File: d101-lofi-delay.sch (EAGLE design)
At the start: 84 parts, among them U1 FX2-20P-1.27DS, U2 FX2-20S-1.27DS

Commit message: Add Knobs
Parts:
- added O2, O3, O4: 450-AA150(15MM,D,BLACK), hardware:450-AA150(15MM,D,BLACK)
- added O5: 450-CP155(15MM,GRAY/WHITE), hardware:450-CP155(15MM,GRAY/WHITE)
- added O6, O7: 450-CP157(15MM,WHITE/BLACK), hardware:450-CP157(15MM,WHITE/BLACK)
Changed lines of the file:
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@@
 <?xml version="1.0" encoding="utf-8"?>
 <!DOCTYPE eagle SYSTEM "eagle.dtd">
-<eagle version="7.4.1">
+<eagle version="7.5.1">
 <drawing>
 <settings>
@@
 <part name="GND24" library="supply" deviceset="GND" device=""/>
 <part name="SA2" library="switches" deviceset="MJS22R" device=""/>
+<part name="O2" library="hardware" deviceset="450-AA?" device="150(15MM,D,BLACK)"/>
+<part name="O3" library="hardware" deviceset="450-AA?" device="150(15MM,D,BLACK)"/>
+<part name="O4" library="hardware" deviceset="450-AA?" device="150(15MM,D,BLACK)"/>
+<part name="O5" library="hardware" deviceset="450-C?" device="P155(15MM,GRAY/WHITE)"/>
+<part name="O6" library="hardware" deviceset="450-C?" device="P157(15MM,WHITE/BLACK)"/>
+<part name="O7" library="hardware" deviceset="450-C?" device="P157(15MM,WHITE/BLACK)"/>
 </parts>
 <sheets>
@@
 <instance part="SA2" gate=".1" x="215.9" y="12.7" rot="MR0"/>
 <instance part="SA2" gate=".2" x="215.9" y="-114.3" rot="MR0"/>
+<instance part="O2" gate="G$1" x="55.88" y="-119.38"/>
+<instance part="O3" gate="G$1" x="289.56" y="-66.04"/>
+<instance part="O4" gate="G$1" x="287.02" y="-193.04"/>
+<instance part="O5" gate="G$1" x="55.88" y="-119.38"/>
+<instance part="O6" gate="G$1" x="289.56" y="-66.04"/>
+<instance part="O7" gate="G$1" x="287.02" y="-193.04"/>
 </instances>
 <busses>

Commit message: Add Knobs
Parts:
- removed C34, C35: 100N, capacitors:100N
- removed C36, C37: 47N(FILM), capacitors:47N(FILM)
- removed C38, C39: 33U/25V, capacitors-electrolytic:33U/25V
- removed O7: 450-CP157(15MM,WHITE/BLACK), hardware:450-CP157(15MM,WHITE/BLACK)
- removed R36, R37, R38, R39: 10K, resistors:10K
- removed R41, R43, R44, R45: 1K, resistors:1K
- added C10, C11: 10N(FILM), capacitors:10N(FILM)
- added C12, C13: 100N, capacitors:100N
- added C8, C9: 100N(FILM), capacitors:100N(FILM)
- added R12, R13, R22, R23: 15K, resistors:15K
- added R14: 1K, resistors:1K
- added R21, R24, R25: 10K, resistors:10K
- added U10: FX2-20S-1.27DS, hardware:FX2-20S-1.27DS
- added U11, U12: D-SHAFT-ADAPTER, hardware:D-SHAFT-ADAPTER
- added U3, U4, U8, U9: NUT-M2-SELFLOCK, hardware:NUT-M2-SELFLOCK
- added U5: FX2-20P-1.27DS, hardware:FX2-20P-1.27DS
- added U6, U7: SCREW-M2X8, hardware:SCREW-M2X8
- C14, C15: value 100N(FILM) -> 2N2(FILM); device capacitors:100N(FILM) -> capacitors:2N2(FILM)
- C16, C17: value 10N(FILM) -> 10U/35V; device capacitors:10N(FILM) -> capacitors-electrolytic:10U/35V
- C18, C19: value 100N -> 2N2(FILM); device capacitors:100N -> capacitors:2N2(FILM)
- C20, C21: value 2N2(FILM) -> 100N(FILM); device capacitors:2N2(FILM) -> capacitors:100N(FILM)
- C22, C23: value 10U/35V -> 10N(FILM); device capacitors-electrolytic:10U/35V -> capacitors:10N(FILM)
- C24, C25: value 2N2(FILM) -> 100N; device capacitors:2N2(FILM) -> capacitors:100N
- C28, C29: value 10N(FILM) -> 100N; device capacitors:10N(FILM) -> capacitors:100N
- C30, C31: value 100N -> 47N(FILM); device capacitors:100N -> capacitors:47N(FILM)
- C32, C33: value 100N(FILM) -> 33U/25V; device capacitors:100N(FILM) -> capacitors-electrolytic:33U/25V
- O1: value (none) -> 450-AA150(15MM,D,BLACK); device text:TITLE -> hardware:450-AA150(15MM,D,BLACK)
- O2: value 450-AA150(15MM,D,BLACK) -> 450-CP155(15MM,GRAY/WHITE); device hardware:450-AA150(15MM,D,BLACK) -> hardware:450-CP155(15MM,GRAY/WHITE)
- O4: value 450-AA150(15MM,D,BLACK) -> 450-CP157(15MM,WHITE/BLACK); device hardware:450-AA150(15MM,D,BLACK) -> hardware:450-CP157(15MM,WHITE/BLACK)
- O5: value 450-CP155(15MM,GRAY/WHITE) -> 450-AA150(15MM,D,BLACK); device hardware:450-CP155(15MM,GRAY/WHITE) -> hardware:450-AA150(15MM,D,BLACK)
- PCB1: value rev.A -> D101 rev.A
- R15, R32: value 15K -> 1K; device resistors:15K -> resistors:1K
- R16: value 15K -> 100K; device resistors:15K -> resistors:100K
- R17: value 1K -> 100K; device resistors:1K -> resistors:100K
- R18: value 1K -> 10K; device resistors:1K -> resistors:10K
- R19, R20: value B50K** -> 10K; device potentiometers:B50K** -> resistors:10K
- R26, R27: value 100K -> 10K; device resistors:100K -> resistors:10K
- R30, R34, R35: value 10K -> 1K; device resistors:10K -> resistors:1K
- R31: value 10K -> B50K**; device resistors:10K -> potentiometers:B50K**
- R33: value 15K -> B50K**; device resistors:15K -> potentiometers:B50K**
- U1: value FX2-20P-1.27DS -> SCREW-M2X8; device hardware:FX2-20P-1.27DS -> hardware:SCREW-M2X8
- U2: value FX2-20S-1.27DS -> SCREW-M2X8; device hardware:FX2-20S-1.27DS -> hardware:SCREW-M2X8
- renumbered SA2 to SA1
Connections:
- net +5V: now also C12.2, C13.2; no longer C18.2, C19.2
- net FBK_INT_LEFT: now also R12.2; no longer R15.2
- net FBK_INT_RIGHT: now also R13.2; no longer R16.2
- net GND: now also C10.1, C11.1, C12.1, C13.1, C16.-, C17.-, C22.1, C23.1, C24.1, C25.1, R16.1, R17.1, R31.CW, R31.W, R33.CW, R33.W, VD1.C, VD4.A; no longer C16.1, C17.1, C18.1, C19.1, C22.-, C23.-, C34.1, C35.1, C36.1, C37.1, R19.CW, R19.W, R20.CW, R20.W, R26.1, R27.1, VD1.A, VD4.C
- net N$1: now also R32.1, R33.CCW; no longer R19.CCW, R43.1
- net N$10: now also C11.2, R19.2, R21.2, R23.2; no longer C17.2, R29.2, R31.2, R33.2
- net N$13: now also R15.1; no longer R18.1
- net N$15: now also C23.2, R25.2, R27.2, R29.2; no longer C29.2, R35.2, R37.2, R39.2
- net N$17: now also C15.2, R23.1; no longer C21.2, R33.1
- net N$18: now also C19.1, R25.1; no longer C25.1, R45.1
- net N$19: now also C19.2, R27.1; no longer C25.2, R37.1
- net N$2: now also R30.1, R31.CCW; no longer R20.CCW, R41.1
- net N$20: now also C21.1, R29.1; no longer C27.1, R39.1
- net N$21: now also C21.2; no longer C27.2
- net N$22: now also C27.1; no longer C33.1
- net N$23: now also C27.2; no longer C33.2
- net N$24: now also C31.2, C33.+, R35.2; no longer C37.2, C39.+, R45.2
- net N$25: now also R13.1; no longer R16.1
- net N$28: now also R3.1; no longer R7.1
- net N$3: now also C9.1, R14.2, VD1.A, VD3.C; no longer C15.1, R17.2, VD1.C, VD2.A
- net N$30: now also R7.1; no longer R2.1
- net N$31: now also C25.2; no longer C31.2
- net N$32: now also C29.2; no longer C35.2
- net N$33: now also R32.2; no longer R43.2
- net N$37: now also C17.+; no longer C23.+
- net N$39: now also R10.2; no longer R8.2
- net N$4: now also C15.1, R21.1; no longer C21.1, R31.1
- net N$40: now also R4.2; no longer R10.2
- net N$48: now also C22.2, R24.2, R26.2, R28.2; no longer C28.2, R34.2, R36.2, R38.2
- net N$49: now also C14.1, R20.1; no longer C20.1, R30.1
- net N$5: now also C8.1, R15.2, VD2.A, VD4.C; no longer C14.1, R18.2, VD3.C, VD4.A
- net N$50: now also C14.2, R22.1; no longer C20.2, R32.1
- net N$51: now also C18.1, R24.1; no longer C24.1, R44.1
- net N$52: now also C18.2, R26.1; no longer C24.2, R36.1
- net N$53: now also C20.1, R28.1; no longer C26.1, R38.1
- net N$54: now also C20.2; no longer C26.2
- net N$55: now also C26.1; no longer C32.1
- net N$56: now also C26.2; no longer C32.2
- net N$57: now also C30.2, C32.+, R34.2; no longer C36.2, C38.+, R44.2
- net N$58: now also C24.2; no longer C30.2
- net N$59: now also C28.2; no longer C34.2
- net N$6: now also R14.1; no longer R17.1
- net N$60: now also R30.2; no longer R41.2
- net N$61: now also R7.2, R8.2; no longer R2.2, R4.2
- net N$62: now also C8.2, R16.2, R18.1; no longer C14.2, R26.2, R28.1
- net N$63: now also C10.2, R18.2, R20.2, R22.2; no longer C16.2, R28.2, R30.2, R32.2
- net N$64: now also R12.1; no longer R15.1
- net N$65: now also R2.2, R8.1; no longer R3.2, R4.1
- net N$69: now also C16.+; no longer C22.+
- net N$7: now also R10.1, R3.2; no longer R7.2, R8.1
- net N$9: now also C9.2, R17.2, R19.1; no longer C15.2, R27.2, R29.1
- net OUT_LEFT: now also C33.-, R4.1; no longer C39.-, R10.1
- net OUT_RIGHT: now also C32.-, R2.1; no longer C38.-, R3.1
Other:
- moved on the sheet: C14, C15, C18, C19, C20, C21, C24, C25, C26, C27, C28, C29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

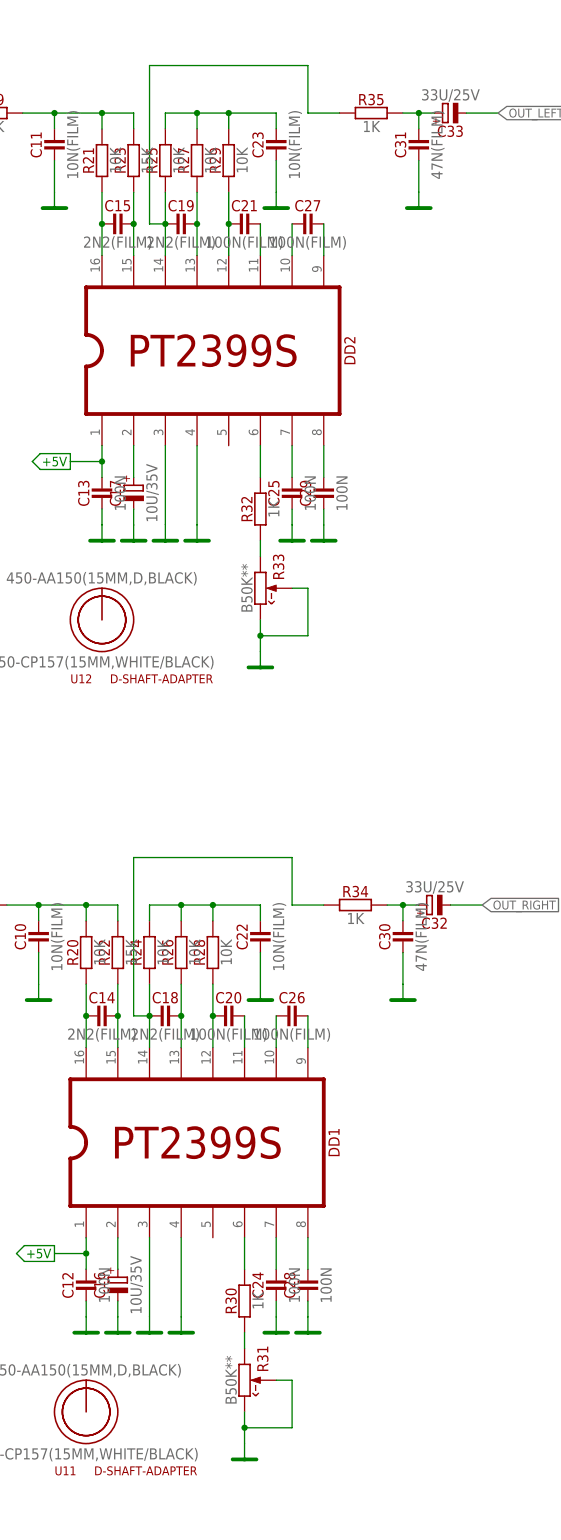
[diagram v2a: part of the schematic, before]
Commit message: D101 Update
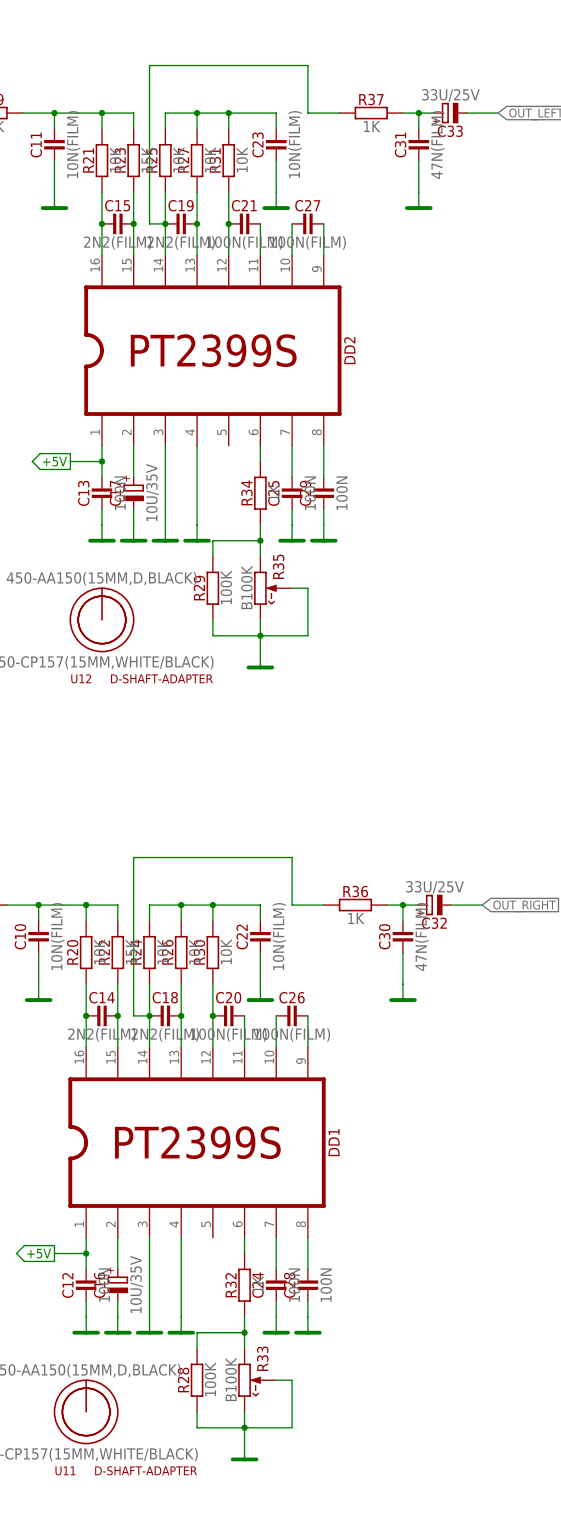
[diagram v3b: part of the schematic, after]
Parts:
- added R36, R37: 1K, resistors:1K
- R28, R29: value 10K -> 100K; device resistors:10K -> resistors:100K
- R30: value 1K -> 10K; device resistors:1K -> resistors:10K
- R31: value B50K** -> 10K; device potentiometers:B50K** -> resistors:10K
- R33: value B50K** -> B100K; device potentiometers:B50K** -> potentiometers:B100K
- R35: value 1K -> B100K; device resistors:1K -> potentiometers:B100K
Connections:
- net GND: now also R28.1, R29.1, R35.CW, R35.W; no longer R31.CW, R31.W
- net N$1: now also R29.2, R34.1, R35.CCW; no longer R32.1, R33.CCW
- net N$15: now also R31.2; no longer R29.2
- net N$18: now also R37.1; no longer R35.1
- net N$2: now also R28.2, R32.1, R33.CCW; no longer R30.1, R31.CCW
- net N$20: now also R31.1; no longer R29.1
- net N$24: now also R37.2; no longer R35.2
- net N$33: now also R34.2; no longer R32.2
- net N$48: now also R30.2; no longer R28.2
- net N$51: now also R36.1; no longer R34.1
- net N$53: now also R30.1; no longer R28.1
- net N$57: now also R36.2; no longer R34.2
- net N$60: now also R32.2; no longer R30.2
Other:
- moved on the sheet: R28, R29, R30, R32, R33, R34

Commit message: PCB Update
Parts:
- removed U11, U12: D-SHAFT-ADAPTER, hardware:D-SHAFT-ADAPTER
- PCB1: value D101 rev.A -> D104 rev.A
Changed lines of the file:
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@@
 </classes>
 <parts>
-<part name="PCB1" library="module-footprints" deviceset="ST2-BOARD-?" device="50" value="D101 rev.A"/>
+<part name="PCB1" library="module-footprints" deviceset="ST2-BOARD-?" device="50" value="D104 rev.A"/>
 <part name="U5" library="hardware" deviceset="?" device="FX2-20P-1.27DS"/>
 <part name="U10" library="hardware" deviceset="?" device="FX2-20S-1.27DS"/>
@@
 <part name="U8" library="hardware" deviceset="*?" device="NUT-M2-SELFLOCK"/>
 <part name="U9" library="hardware" deviceset="*?" device="NUT-M2-SELFLOCK"/>
-<part name="U12" library="hardware" deviceset="*?" device="D-SHAFT-ADAPTER"/>
-<part name="U11" library="hardware" deviceset="*?" device="D-SHAFT-ADAPTER"/>
 <part name="R29" library="resistors" deviceset="?" device="100K"/>
 <part name="R28" library="resistors" deviceset="?" device="100K"/>
@@
 <instance part="U8" gate="G$1" x="132.08" y="15.24"/>
 <instance part="U9" gate="G$1" x="132.08" y="12.7"/>
-<instance part="U12" gate="G$1" x="284.48" y="-76.2"/>
-<instance part="U11" gate="G$1" x="281.94" y="-203.2"/>
 <instance part="R29" gate="G$1" x="307.34" y="-60.96" rot="R90"/>
 <instance part="R28" gate="G$1" x="304.8" y="-187.96" rot="R90"/>
